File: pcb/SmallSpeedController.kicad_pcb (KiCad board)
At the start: 4 copper layers, 30.7 x 51.7 mm, 38 parts, among them J1 Conn_01x02_Socket, J10 Conn_01x03_Socket, J11 Conn_01x03_Socket, J2 Conn_01x02_Socket, J4 Conn_01x02_Socket, J5 Conn_01x04_Socket, J6 Conn_01x04_Socket, J9 Conn_01x03_Socket, SW2 TS-1088-AR02016, U2 AMS1117-3.3, U3 DRV8837DSGR, U4 DRV8837DSGR, U5 CH32V003FxUx

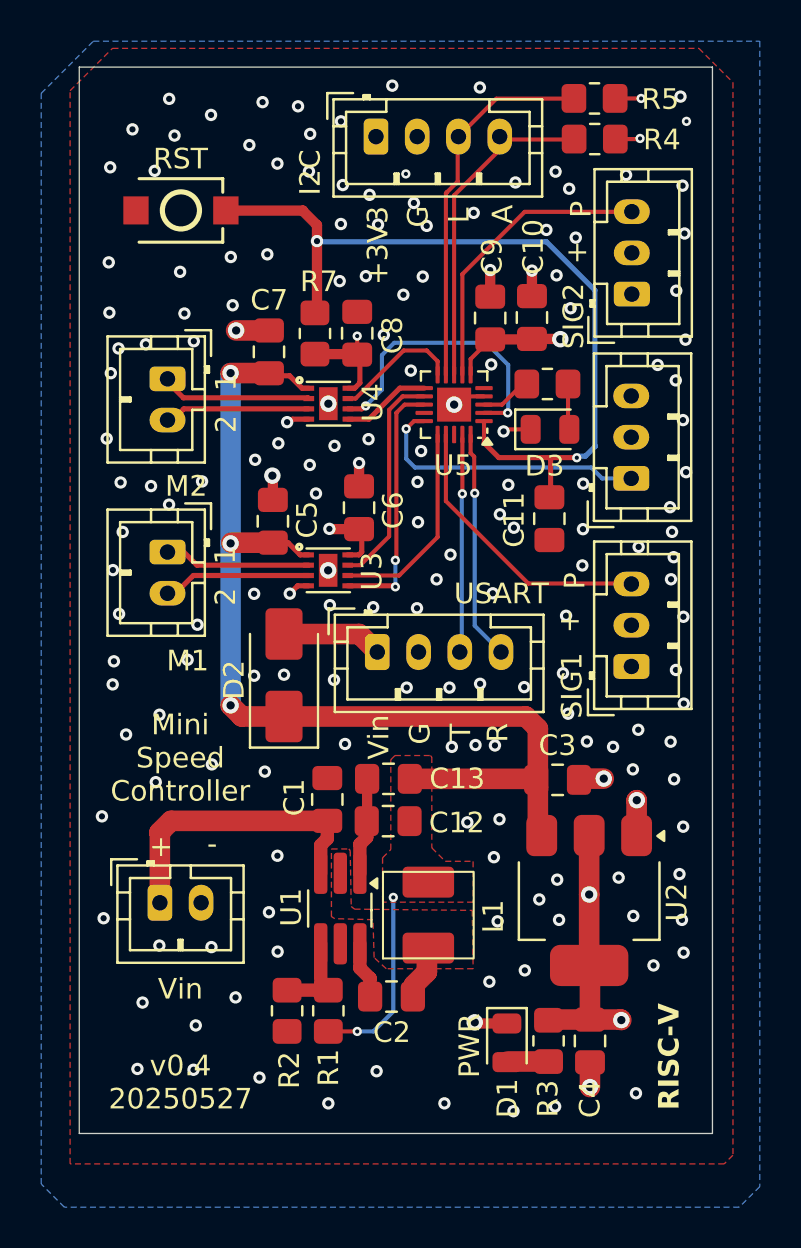
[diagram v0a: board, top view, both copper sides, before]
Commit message: pcb: smaller board optimizations, no functional changes
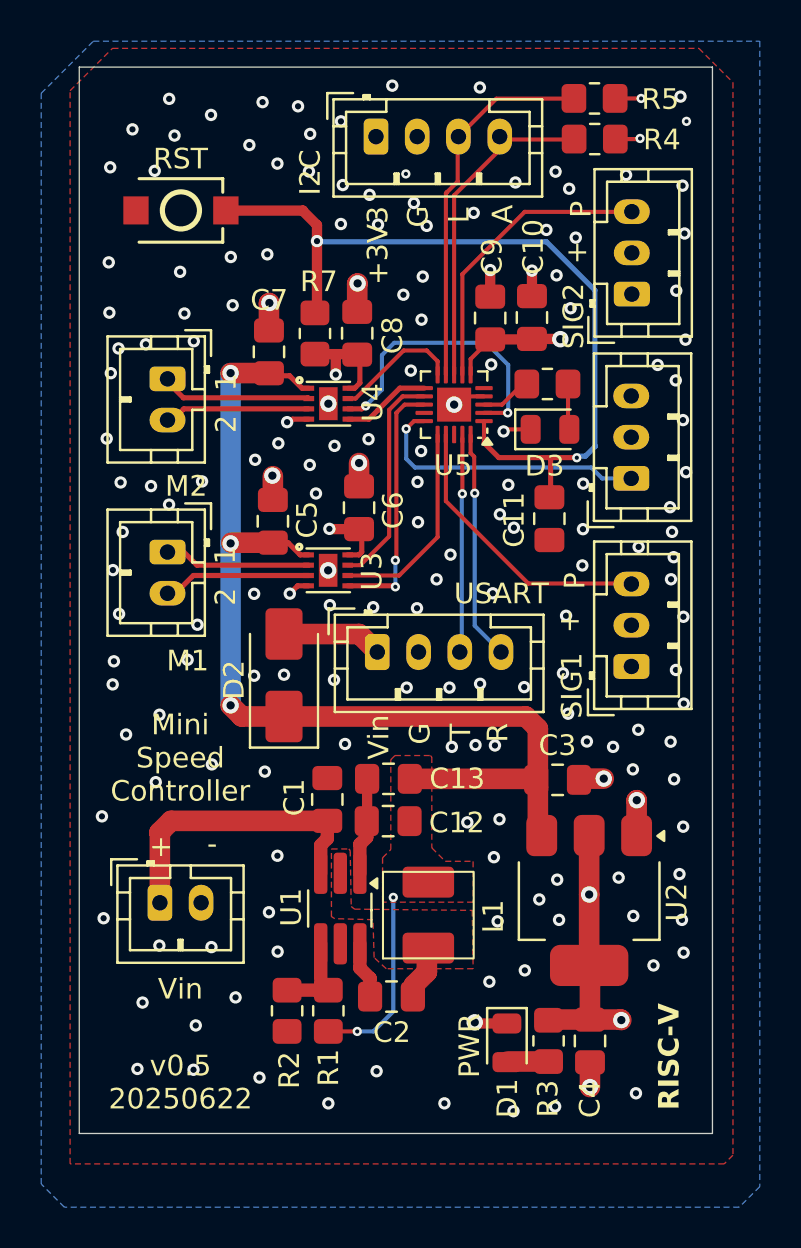
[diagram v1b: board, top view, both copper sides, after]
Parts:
- C11: value C -> 100nF
- U1: value ~ -> AP62300TWU
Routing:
- net GND: track 21.4 -> 22.5 mm, vias 176 -> 175
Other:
- board text added: "v0.5 20250622"
- board text removed: "v0.4 20250527"
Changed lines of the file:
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@@
 			)
 		)
-		(property "Value" "C"
+		(property "Value" "100nF"
 			(at 0 1.68 90)
 			(layer "F.Fab")
@@
 			)
 		)
-		(property "Value" "~"
+		(property "Value" "AP62300TWU"
 			(at 0 2.5 90)
 			(layer "F.Fab")
@@
 		)
 	)
-	(gr_text "v0.4\n20250527"
+	(gr_text "v0.5\n20250622"
 		(at 24.43 118.91 0)
 		(layer "F.SilkS")
@@
 		(start 33.09 88.6125)
 		(end 33.09 87.4825)
-		(width 0.5)
+		(width 1)
 		(layer "F.Cu")
 		(net 2)
@@
 	)
 	(segment
+		(start 33 80.15)
+		(end 33 78.79)
+		(width 1)
+		(layer "F.Cu")
+		(net 2)
+	)
+	(segment
 		(start 39.15 84.25)
 		(end 38.1 84.25)
@@
 	)
 	(segment
+		(start 28.72 81.0525)
+		(end 28.72 79.74)
+		(width 1)
+		(layer "F.Cu")
+		(net 2)
+	)
+	(segment
 		(start 33.13 105.97)
 		(end 33.13 107.38)
@@
 		(start 28.91 89.27)
 		(end 28.91 88.12)
-		(width 0.5)
+		(width 1)
 		(layer "F.Cu")
 		(net 2)
 	)
 	(segment
-		(start 28.72 81.0525)
-		(end 27.1275 81.0525)
+		(start 28.72 79.74)
+		(end 28.74 79.72)
+		(width 1)
+		(layer "F.Cu")
+		(net 2)
+	)
+	(segment
+		(start 33 78.79)
+		(end 33.02 78.77)
 		(width 1)
 		(layer "F.Cu")
@@
 	(via
 		(at 33.09 87.4825)
-		(size 0.6)
-		(drill 0.3)
+		(size 0.8)
+		(drill 0.4)
 		(layers "F.Cu" "B.Cu")
 		(net 2)
@@
 	)
 	(via
-		(at 27.1275 81.0525)
+		(at 28.74 79.72)
 		(size 0.8)
 		(drill 0.4)
@@
 	)
 	(via
-		(at 33.42 78.42)
-		(size 0.6)
-		(drill 0.3)
-		(layers "F.Cu" "B.Cu")
-		(free yes)
-		(net 2)
-	)
-	(via
 		(at 27.1 113.4)
 		(size 0.6)
@@
 	)
 	(via
-		(at 32.15 78.66)
-		(size 0.6)
-		(drill 0.3)
-		(layers "F.Cu" "B.Cu")
-		(free yes)
-		(net 2)
-	)
-	(via
 		(at 37.475 98.375)
 		(size 0.6)
@@
 	)
 	(via
+		(at 33.02 78.77)
+		(size 0.8)
+		(drill 0.4)
+		(layers "F.Cu" "B.Cu")
+		(net 2)
+	)
+	(via
 		(at 40.6 90.62)
 		(size 0.6)
@@
 	)
 	(via
-		(at 34.29 81.27)
+		(at 36.12 80.53)
 		(size 0.6)
 		(drill 0.3)
@@
 	)
 	(segment
-		(start 30.95 82.2)
+		(start 31.96 82.25)
+		(end 32.01 82.2)
+		(width 0.5)
+		(layer "F.Cu")
+		(net 3)
+	)
+	(segment
+		(start 32.01 82.2)
 		(end 32.975 82.2)
 		(width 0.5)
@@
 	)
 	(segment
+		(start 30.95 82.2)
+		(end 32.01 82.2)
+		(width 0.5)
+		(layer "F.Cu")
+		(net 3)
+	)
+	(segment
 		(start 32.54 91.9375)
 		(end 33.0825 91.9375)
@@
 	)
 	(segment
-		(start 33 81.325)
-		(end 33 82.225)
-		(width 0.2)
-		(layer "F.Cu")
-		(net 3)
-	)
-	(segment
 		(start 44.25 108.41)
 		(end 44.25 111.85)
@@
 		(net 3)
 	)
+	(segment
+		(start 31.96 83.19)
+		(end 31.96 82.25)
+		(width 0.5)
+		(layer "F.Cu")
+		(net 3)
+	)
 	(via
 		(at 45.81 114.5)
@@
 	)
 	(via
-		(at 33 81.325)
-		(size 0.45)
-		(drill 0.2)
-		(layers "F.Cu" "B.Cu")
-		(net 3)
-	)
-	(via
 		(at 46.77 69.8)
 		(size 0.45)
@@
 		(net 3)
 	)
+	(via
+		(at 31.96 83.19)
+		(size 0.6)
+		(drill 0.3)
+		(layers "F.Cu" "B.Cu")
+		(net 3)
+	)
 	(segment
 		(start 31.05 76.72)
@@
 	)
 	(segment
-		(start 38.699324 88.946461)
-		(end 38.675 88.922137)
+		(start 38.675 87.175)
+		(end 38.5 87)
 		(width 0.2)
 		(layer "F.Cu")
@@
 	)
 	(segment
-		(start 38.675 87.175)
-		(end 38.5 87)
+		(start 38.675 88.922137)
+		(end 38.675 87.175)
 		(width 0.2)
 		(layer "F.Cu")
@@
 	)
 	(segment
-		(start 38.5 87)
-		(end 38.5 86.125)
+		(start 38.699324 88.946461)
+		(end 38.675 88.922137)
 		(width 0.2)
 		(layer "F.Cu")
@@
 	)
 	(segment
-		(start 38.675 88.922137)
-		(end 38.675 87.175)
+		(start 38.5 87)
+		(end 38.5 86.125)
 		(width 0.2)
 		(layer "F.Cu")
@@
 	)
 	(segment
-		(start 38.7 95.375)
-		(end 39.975 96.65)
+		(start 38.771458 88.946461)
+		(end 38.7 89.017919)
 		(width 0.2)
 		(layer "B.Cu")
@@
 	)
 	(segment
-		(start 38.699324 88.946461)
-		(end 38.771458 88.946461)
+		(start 38.7 89.017919)
+		(end 38.7 95.375)
 		(width 0.2)
 		(layer "B.Cu")
@@
 	)
 	(segment
-		(start 38.771458 88.946461)
-		(end 38.7 89.017919)
+		(start 38.7 95.375)
+		(end 39.975 96.65)
 		(width 0.2)
 		(layer "B.Cu")
@@
 	)
 	(segment
-		(start 38.7 89.017919)
-		(end 38.7 95.375)
+		(start 38.699324 88.946461)
+		(end 38.771458 88.946461)
 		(width 0.2)
 		(layer "B.Cu")
